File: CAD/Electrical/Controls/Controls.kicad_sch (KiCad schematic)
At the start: 49 parts, among them J1 Elevator Servo, J10 Battery and/or BMS, J11 Restart/Boot Button, J12 GPS, J13 Cadence Sensor, J14 Gyroscope, J15 LCD, J16 pitot tube assembly, J17 SD card selecting jumper, J19 Rudder Servo, J2 SD card, J20 Elevron/Spoliron Servo, J21 Elevron/Spoliron Servo, J22 SD card selecting jumper, J3 External Connector, J4 Rudder Servo, J5 Elevator Servo, J6 BME280, J7 Pitch Control, J8 Roll Control, Q1 2N3904, Q2 2N3905, U1 ESP32-C3-DevKitM-1, U2 5V regulator, U3 3-6V to 6V DC/DC converter, U8 3V3 regulator, U9 ESP32-WROOM-32E

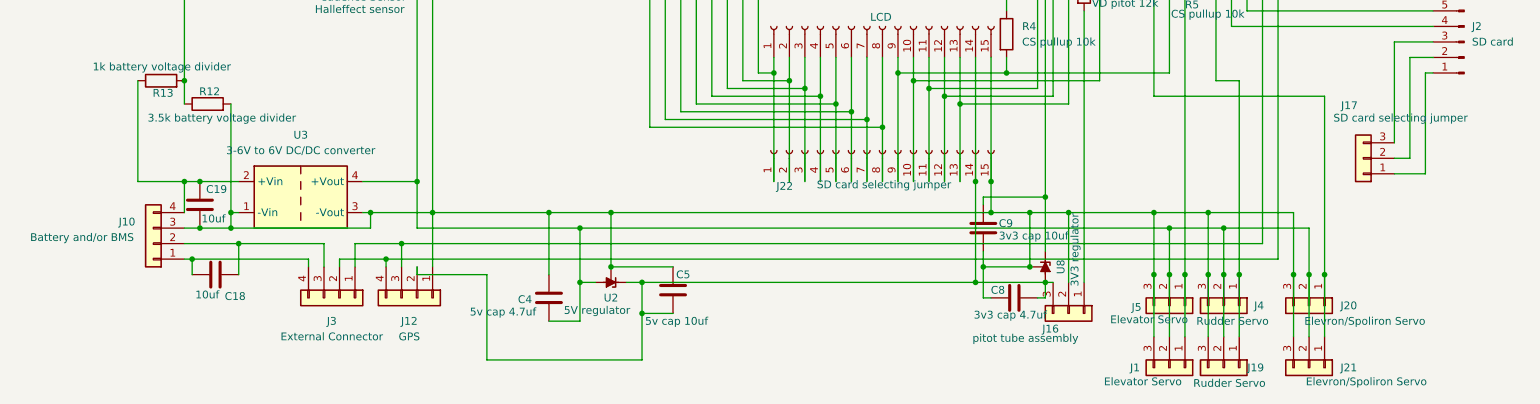
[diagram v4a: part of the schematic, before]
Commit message: update
soon to break up the schematic
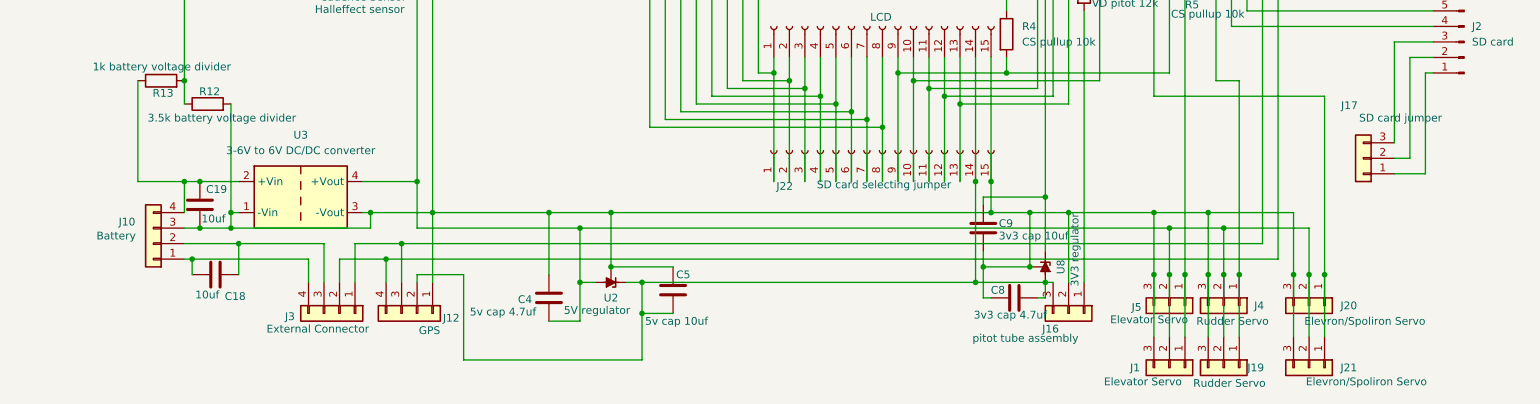
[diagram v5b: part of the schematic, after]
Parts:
- J10: value Battery and/or BMS -> Battery
- J17: value SD card selecting jumper -> SD card jumper
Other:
- moved on the sheet: J12, J3
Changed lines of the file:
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@@
 	(wire
 		(pts
-			(xy 64.77 158.75) (xy 64.77 160.02)
+			(xy 64.77 158.75) (xy 64.77 162.56)
 		)
 		(stroke
@@
 	(wire
 		(pts
-			(xy 52.07 160.02) (xy 52.07 158.75)
+			(xy 52.07 162.56) (xy 52.07 158.75)
 		)
 		(stroke
@@
 	(wire
 		(pts
-			(xy 69.85 161.29) (xy 69.85 160.02)
+			(xy 69.85 161.29) (xy 69.85 162.56)
 		)
 		(stroke
@@
 	(wire
 		(pts
-			(xy 69.85 161.29) (xy 81.28 161.29)
+			(xy 69.85 161.29) (xy 77.47 161.29)
 		)
 		(stroke
@@
 	(wire
 		(pts
-			(xy 67.31 156.21) (xy 67.31 160.02)
+			(xy 67.31 156.21) (xy 67.31 162.56)
 		)
 		(stroke
@@
 	(wire
 		(pts
-			(xy 57.15 158.75) (xy 57.15 160.02)
+			(xy 57.15 158.75) (xy 57.15 162.56)
 		)
 		(stroke
@@
 	(wire
 		(pts
-			(xy 54.61 160.02) (xy 54.61 156.21)
+			(xy 54.61 162.56) (xy 54.61 156.21)
 		)
 		(stroke
@@
 	(wire
 		(pts
-			(xy 72.39 151.13) (xy 72.39 160.02)
+			(xy 72.39 151.13) (xy 72.39 162.56)
 		)
 		(stroke
@@
 	(wire
 		(pts
-			(xy 59.69 156.21) (xy 59.69 160.02)
+			(xy 59.69 156.21) (xy 59.69 162.56)
 		)
 		(stroke
@@
 	(wire
 		(pts
-			(xy 81.28 161.29) (xy 81.28 175.26)
+			(xy 77.47 161.29) (xy 77.47 175.26)
 		)
 		(stroke
@@
 	(wire
 		(pts
-			(xy 81.28 175.26) (xy 106.68 175.26)
+			(xy 77.47 175.26) (xy 106.68 175.26)
 		)
 		(stroke
@@
 	(symbol
 		(lib_id "Connector_Generic:Conn_01x04")
-		(at 69.85 165.1 270)
+		(at 69.85 167.64 270)
 		(unit 1)
 		(exclude_from_sim no)
@@
 		(on_board yes)
 		(dnp no)
-		(fields_autoplaced yes)
 		(property "Reference" "J12"
-			(at 68.58 168.91 90)
+			(at 75.438 168.402 90)
 			(effects
 				(font
@@
 		)
 		(property "Value" "GPS"
-			(at 68.58 171.45 90)
+			(at 71.882 170.434 90)
 			(effects
 				(font
@@
 		)
 		(property "Footprint" "Connector_Molex:Molex_KK-254_AE-6410-04A_1x04_P2.54mm_Vertical"
-			(at 69.85 165.1 0)
+			(at 69.85 167.64 0)
 			(effects
 				(font
@@
 		)
 		(property "Datasheet" "~"
-			(at 69.85 165.1 0)
+			(at 69.85 167.64 0)
 			(effects
 				(font
@@
 		)
 		(property "Description" "Generic connector, single row, 01x04, script generated (kicad-library-utils/schlib/autogen/connector/)"
-			(at 69.85 165.1 0)
+			(at 69.85 167.64 0)
 			(effects
 				(font
@@
 	(symbol
 		(lib_id "Connector_Generic:Conn_01x04")
-		(at 57.15 165.1 270)
+		(at 57.15 167.64 270)
 		(unit 1)
 		(exclude_from_sim no)
@@
 		(on_board yes)
 		(dnp no)
-		(fields_autoplaced yes)
 		(property "Reference" "J3"
-			(at 55.88 168.91 90)
+			(at 49.022 168.148 90)
 			(effects
 				(font
@@
 		)
 		(property "Value" "External Connector"
-			(at 55.88 171.45 90)
+			(at 53.594 170.18 90)
 			(effects
 				(font
@@
 		)
 		(property "Footprint" "Connector_Molex:Molex_KK-254_AE-6410-04A_1x04_P2.54mm_Vertical"
-			(at 57.15 165.1 0)
+			(at 57.15 167.64 0)
 			(effects
 				(font
@@
 		)
 		(property "Datasheet" "~"
-			(at 57.15 165.1 0)
+			(at 57.15 167.64 0)
 			(effects
 				(font
@@
 		)
 		(property "Description" "Generic connector, single row, 01x04, script generated (kicad-library-utils/schlib/autogen/connector/)"
-			(at 57.15 165.1 0)
+			(at 57.15 167.64 0)
 			(effects
 				(font
@@
 			)
 		)
-		(property "Value" "SD card selecting jumper"
+		(property "Value" "SD card jumper"
 			(at 230.886 135.636 0)
 			(effects
@@
 			)
 		)
-		(property "Value" "Battery and/or BMS"
-			(at 14.986 155.194 0)
+		(property "Value" "Battery"
+			(at 20.574 154.94 0)
 			(effects
 				(font
